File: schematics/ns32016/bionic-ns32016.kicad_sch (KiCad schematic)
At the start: 12 parts, among them J1 Bionic-P135, J2 Bionic-P245, U1 NS32016N, U2 74HCT126, U3 74HCT541, U4 74HCT541, U5 11AA010-I/TO

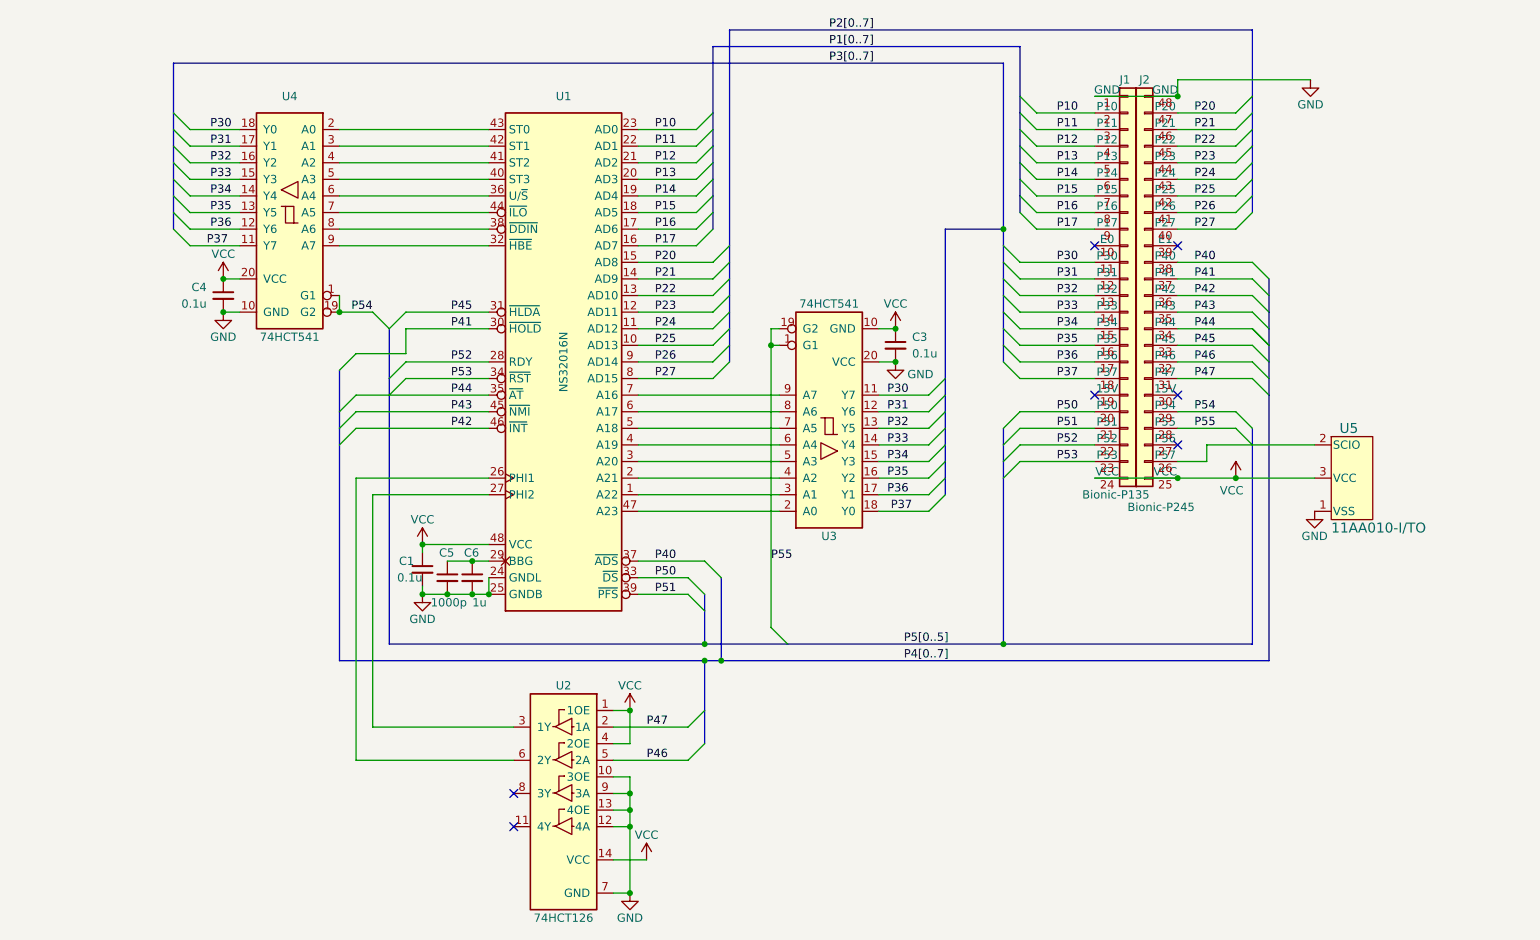
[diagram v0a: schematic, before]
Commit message: [WIP] [NS32016] Update schematics
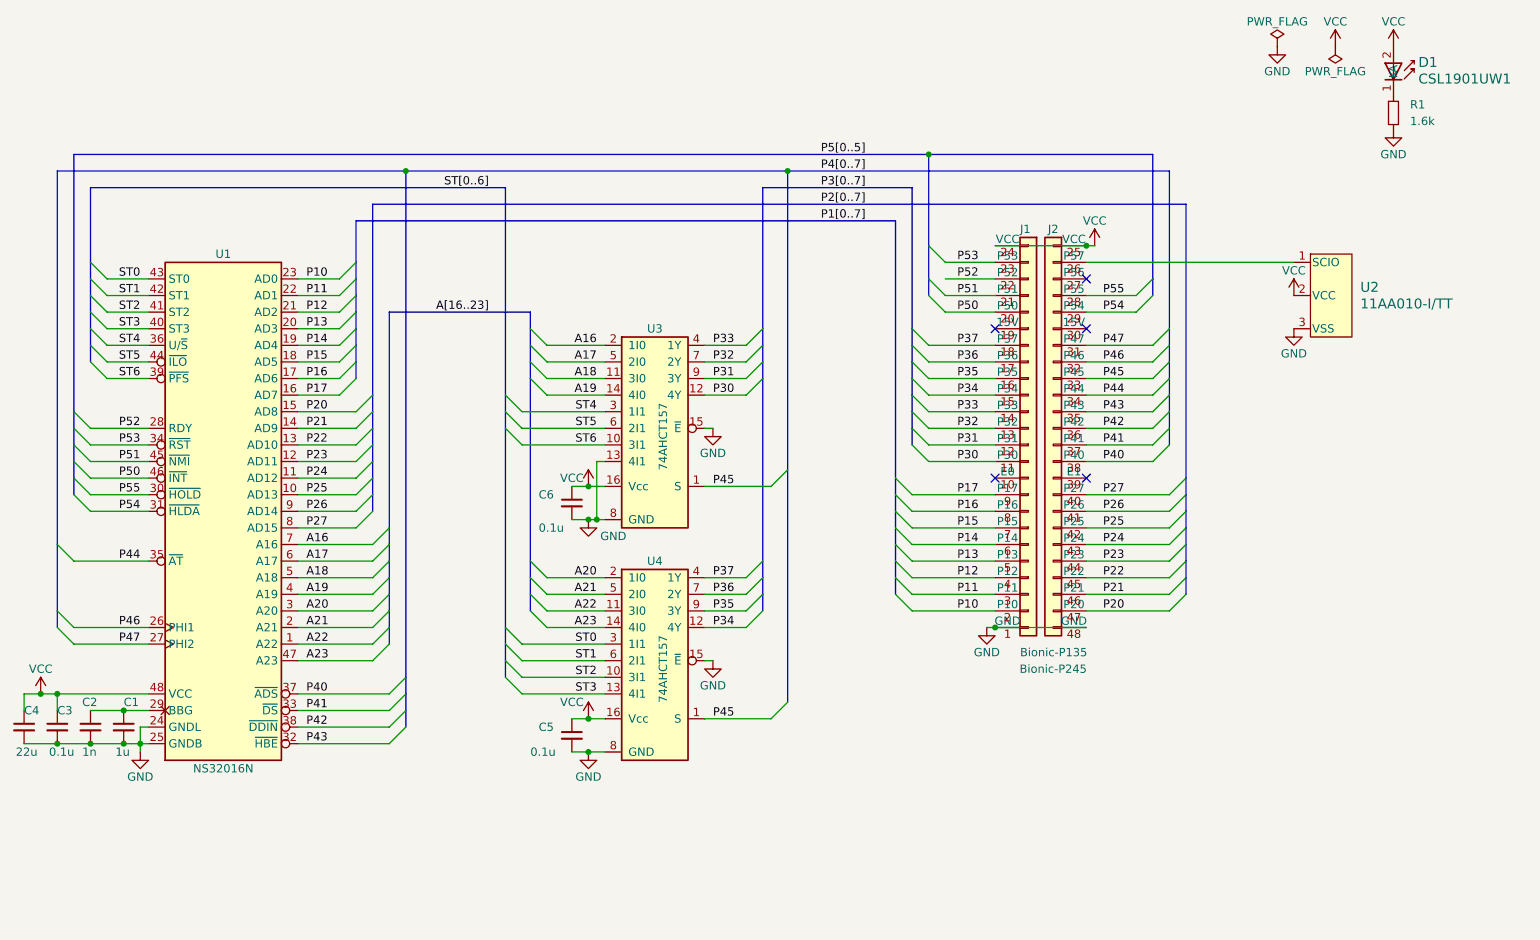
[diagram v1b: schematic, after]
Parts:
- removed J1: Bionic-P135, connector:Bionic-P135_Vertical, symbol 0-LocalLibrary:Bionic-P135
- removed J2: Bionic-P245, connector:Bionic-P245_Vertical, symbol 0-LocalLibrary:Bionic-P245
- removed U1: NS32016N, Package_DIP:DIP-48_W15.24mm, symbol 0-LocalLibrary:NS32016N
- removed U2: 74HCT126, Package_DIP:DIP-14_W7.62mm, symbol 0-LocalLibrary:74HCT126
- removed U3, U4: 74HCT541, Package_DIP:DIP-20_W7.62mm, symbol 0-LocalLibrary:74HCT541
- removed U5: 11AA010-I/TO, TO-92_MC_MCH, symbol 0-LocalLibrary:11AA010-I_TO
- added C2: 1n, Capacitor_SMD:C_0603_1608Metric_Pad1.08x0.95mm_HandSolder, symbol Device:C_Small
- added D1: CSL1901UW1, rhom:LED_CSL1901UW1_ROM-M, symbol rhom:CSL1901UW1
- added J1: Bionic-P135, bionic:Bionic-P135_Vertical, symbol bionic:Bionic-P135
- added J2: Bionic-P245, bionic:Bionic-P245_Vertical, symbol bionic:Bionic-P245
- added R1: 1.6k, Resistor_SMD:R_0603_1608Metric_Pad0.98x0.95mm_HandSolder, symbol Device:R_Small
- added U1: NS32016N, bionic:DIP-48_W15.24mm_Socket, symbol cpu:NS32016N
- added U2: 11AA010-I/TT, microchip:SOT-23_MC_MCH-M, symbol microchip:11AA010-I_TT
- added U3, U4: 74AHCT157, ti:PW16-M, symbol ti:74AHCT157
- C1: value 0.1u -> 1u; footprint Capacitor_THT:C_Disc_D3.4mm_W2.1mm_P2.50mm -> Capacitor_SMD:C_0603_1608Metric_Pad1.08x0.95mm_HandSolder
- C3: footprint Capacitor_THT:C_Disc_D3.4mm_W2.1mm_P2.50mm -> Capacitor_SMD:C_0603_1608Metric_Pad1.08x0.95mm_HandSolder
- C4: value 0.1u -> 22u; footprint Capacitor_THT:C_Disc_D3.4mm_W2.1mm_P2.50mm -> Capacitor_SMD:C_0603_1608Metric_Pad1.08x0.95mm_HandSolder
- C5: value 1000p -> 0.1u; footprint Capacitor_THT:C_Disc_D3.4mm_W2.1mm_P2.50mm -> Capacitor_SMD:C_0603_1608Metric_Pad1.08x0.95mm_HandSolder
- C6: value 1u -> 0.1u; footprint Capacitor_THT:C_Disc_D3.4mm_W2.1mm_P2.50mm -> Capacitor_SMD:C_0603_1608Metric_Pad1.08x0.95mm_HandSolder
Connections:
- net GND: now also C2.2, J1.1 (GND), J2.48 (GND), R1.2, U1.24 (GNDL), U1.25 (GNDB), U2.3 (VSS), U3.13 (4I1), U3.15 (~{E}), U3.8 (GND), U4.15 (~{E}), U4.8 (GND)
- net P10: now also J1.2 (P10), U1.23 (AD0)
- net P11: now also J1.3 (P11), U1.22 (AD1)
- net P12: now also J1.4 (P12), U1.21 (AD2)
- net P13: now also J1.5 (P13), U1.20 (AD3)
- net P14: now also J1.6 (P14), U1.19 (AD4)
- net P15: now also J1.7 (P15), U1.18 (AD5)
- net P16: now also J1.8 (P16), U1.17 (AD6)
- net P17: now also J1.9 (P17), U1.16 (AD7)
- net P20: now also J2.47 (P20), U1.15 (AD8)
- net P21: now also J2.46 (P21), U1.14 (AD9)
- net P22: now also J2.45 (P22), U1.13 (AD10)
- net P23: now also J2.44 (P23), U1.12 (AD11)
- net P24: now also J2.43 (P24), U1.11 (AD12)
- net P25: now also J2.42 (P25), U1.10 (AD13)
- net P26: now also J2.41 (P26), U1.9 (AD14)
- net P27: now also J2.40 (P27), U1.8 (AD15)
- net P30: now also J1.11 (P30), U3.12 (4Y)
- net P31: now also J1.12 (P31), U3.9 (3Y)
- net P32: now also J1.13 (P32), U3.7 (2Y)
- net P33: now also J1.14 (P33), U3.4 (1Y)
- net P34: now also J1.15 (P34), U4.12 (4Y)
- net P35: now also J1.16 (P35), U4.9 (3Y)
- net P36: now also J1.17 (P36), U4.7 (2Y)
- net P37: now also J1.18 (P37), U4.4 (1Y)
- net P40: now also J2.38 (P40), U1.37 (~{ADS})
- net P41: now also J2.37 (P41), U1.33 (~{DS})
- net P42: now also J2.36 (P42), U1.38 (~{DDIN})
- net P43: now also J2.35 (P43), U1.32 (~{HBE})
- net P44: now also J2.34 (P44), U1.35 (~{AT})
- net P45: now also J2.33 (P45), U3.1 (S), U4.1 (S)
- net P46: now also J2.32 (P46), U1.26 (PHI1)
- net P47: now also J2.31 (P47), U1.27 (PHI2)
- net P50: now also J1.20 (P50), U1.46 (~{INT})
- net P51: now also J1.21 (P51), U1.45 (~{NMI})
- net P52: now also J1.22 (P52), U1.28 (RDY)
- net P53: now also J1.23 (P53), U1.34 (~{RST})
- net P54: now also J2.29 (P54), U1.31 (~{HLDA})
- net P55: now also J2.28 (P55), U1.30 (~{HOLD})
- net VCC: now also C5.1, C6.1, D1.2 (A), J1.24 (VCC), J2.25 (VCC), U1.48 (VCC), U2.2 (VCC), U3.16 (Vcc), U4.16 (Vcc); no longer C1.1
- new net: J2.26 (P57), U2.1 (SCIO)
- new net: D1.1 (K), R1.1
- new net: C1.1, C2.1, U1.29 (BBG)
- new net A16: U1.7 (A16), U3.2 (1I0)
- new net A17: U1.6 (A17), U3.5 (2I0)
- new net A18: U1.5 (A18), U3.11 (3I0)
- new net A19: U1.4 (A19), U3.14 (4I0)
- new net A20: U1.3 (A20), U4.2 (1I0)
- new net A21: U1.2 (A21), U4.5 (2I0)
- new net A22: U1.1 (A22), U4.11 (3I0)
- new net A23: U1.47 (A23), U4.14 (4I0)
- new net ST0: U1.43 (ST0), U4.3 (1I1)
- new net ST1: U1.42 (ST1), U4.6 (2I1)
- new net ST2: U1.41 (ST2), U4.10 (3I1)
- new net ST3: U1.40 (ST3), U4.13 (4I1)
- new net ST4: U1.36 (U/~{S}), U3.3 (1I1)
- new net ST5: U1.44 (~{ILO}), U3.6 (2I1)
- new net ST6: U1.39 (~{PFS}), U3.10 (3I1)
- no-connect marks 7 -> 5

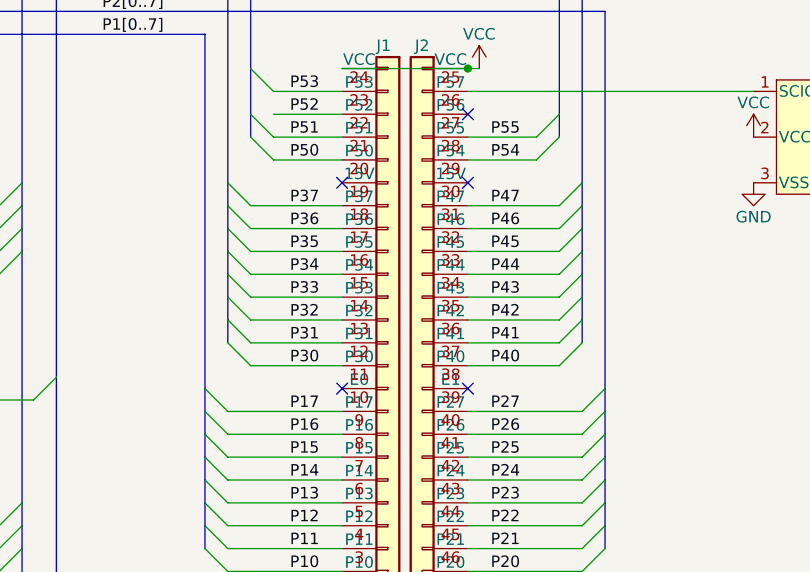
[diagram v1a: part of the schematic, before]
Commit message: [WIP] [NS32016] Use SMT connector
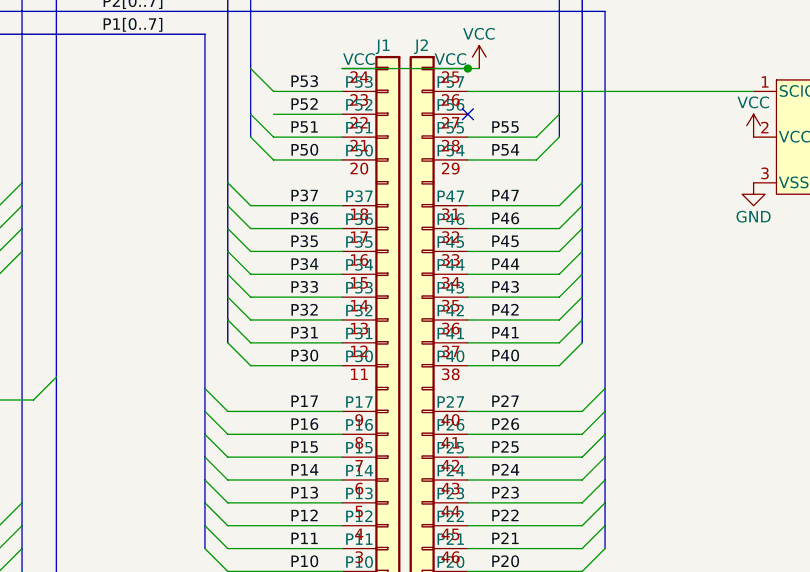
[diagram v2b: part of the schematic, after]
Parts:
- J1: footprint bionic:Bionic-P135_Vertical -> bionic:Bionic-P135_SMT
- J2: footprint bionic:Bionic-P245_Vertical -> bionic:Bionic-P245_SMT
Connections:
- no-connect marks 5 -> 1
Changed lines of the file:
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@@
 	(title_block
 		(title "BionicNS32016")
-		(date "2024-11-04")
+		(date "2025-02-27")
 		(rev "2")
 		(company "Tadashi G. Takaoka")
@@
 	)
 	(no_connect
-		(at 186.69 104.14)
-	)
-	(no_connect
-		(at 200.66 81.28)
-	)
-	(no_connect
-		(at 186.69 81.28)
-	)
-	(no_connect
-		(at 200.66 104.14)
-	)
-	(no_connect
 		(at 200.66 73.66)
 	)
@@
 			)
 		)
-		(property "Footprint" "bionic:Bionic-P245_Vertical"
+		(property "Footprint" "bionic:Bionic-P245_SMT"
 			(at 200.66 132.08 0)
 			(effects
@@
 		(pin "47"
 		)
-		(pin "39"
-		)
 		(pin "32"
 		)
@@
 		(pin "33"
 		)
-		(pin "30"
-		)
 		(pin "36"
 		)
@@
 			)
 		)
-		(property "Footprint" "bionic:Bionic-P135_Vertical"
+		(property "Footprint" "bionic:Bionic-P135_SMT"
 			(at 193.04 132.08 0)
 			(effects
@@
 		(pin "20"
 		)
-		(pin "19"
-		)
 		(pin "9"
 		)
@@
 		(pin "13"
 		)
-		(pin "10"
-		)
 		(instances
